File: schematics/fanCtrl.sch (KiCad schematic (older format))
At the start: 0 parts

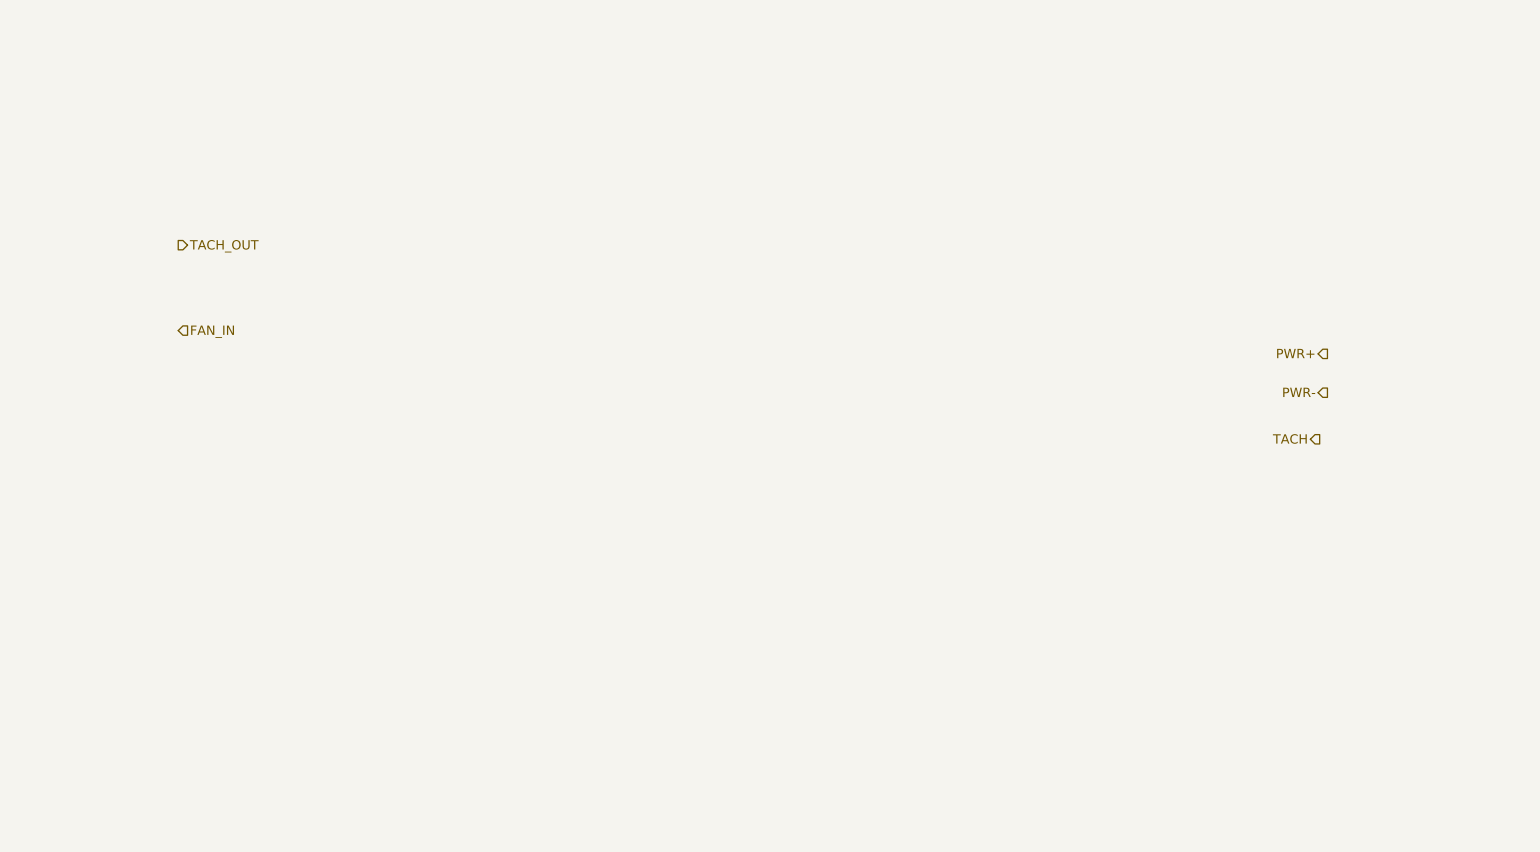
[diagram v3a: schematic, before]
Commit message: added basic current source
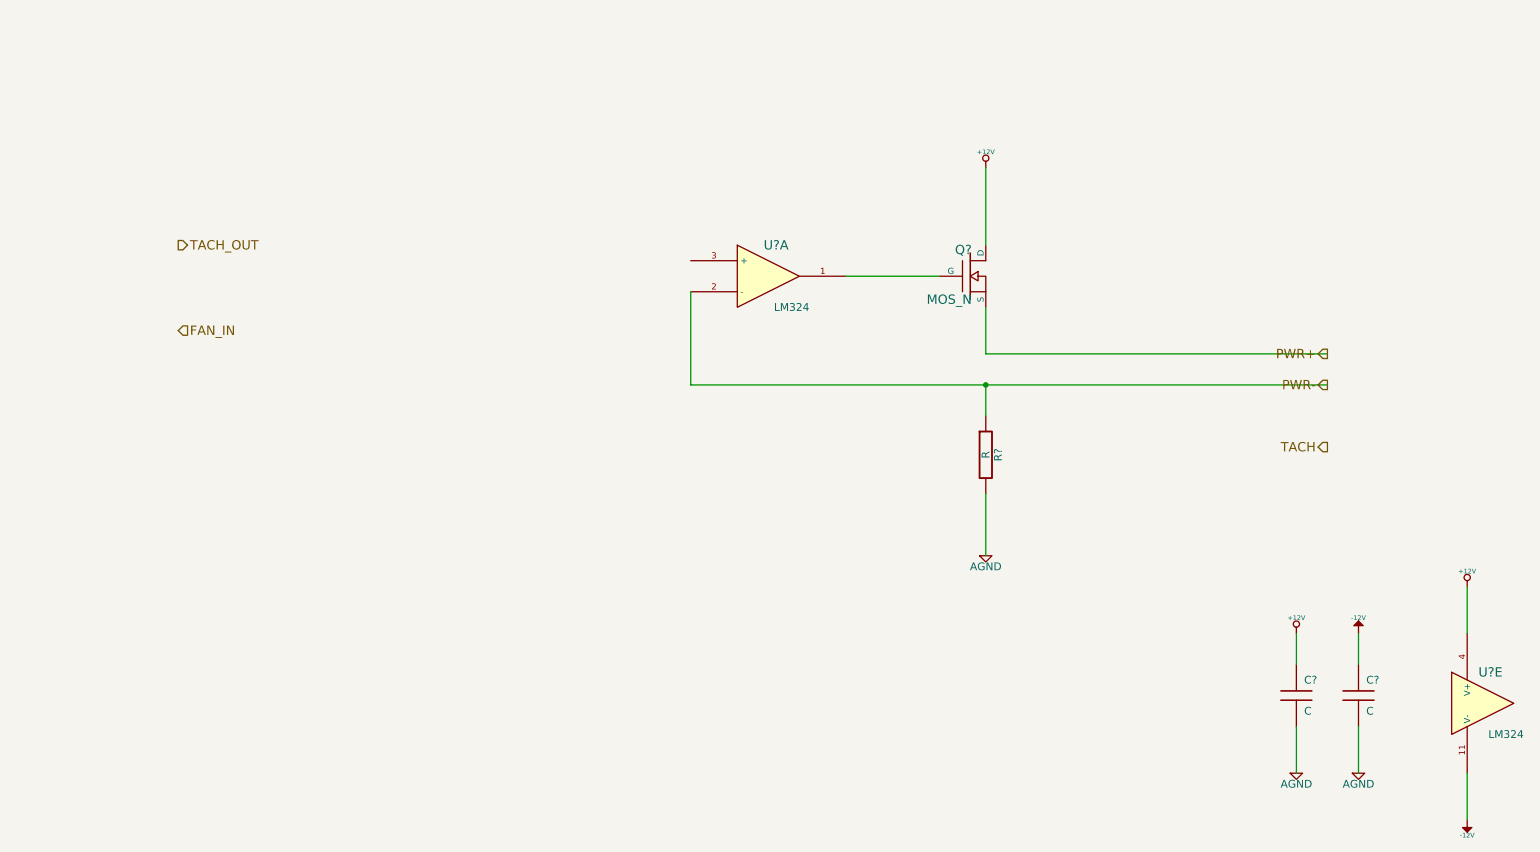
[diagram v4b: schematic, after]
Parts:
- added C? (x2): C, symbol C
- added Q?: MOS_N, symbol MOS_N
- added R?: R, symbol R
- added U? (x2): LM324, symbol LM324
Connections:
- net PWR+: now also Q?.S
- net PWR-: now also R?.1, U?.2 (-)
- new net: Q?.G, U?.1
- new net +12V: C?.1, Q?.D, U?.4 (V+)
- new net -12V: C?.1, U?.11 (V-)
- new net AGND: C?.2, C?.2, R?.2
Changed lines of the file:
@@
-EESchema Schematic File Version 2  date Sat 05 Oct 2013 09:15:56 PM EDT
+EESchema Schematic File Version 2  date Sat 05 Oct 2013 09:39:23 PM EDT
 LIBS:power
 LIBS:device
@@
 Comment4 ""
 $EndDescr
+Wire Wire Line
+	9000 5200 9000 5500
+Wire Wire Line
+	8600 4800 8600 4600
+Wire Wire Line
+	9700 4300 9700 4600
+Connection ~ 6600 3000
+Wire Wire Line
+	4700 2400 4700 3000
+Wire Wire Line
+	4700 3000 8800 3000
+Wire Wire Line
+	6600 3000 6600 3200
+Wire Wire Line
+	6600 1600 6600 2100
+Wire Wire Line
+	6300 2300 5700 2300
+Wire Wire Line
+	8800 2800 6600 2800
+Wire Wire Line
+	6600 2800 6600 2500
+Wire Wire Line
+	6600 4100 6600 3700
+Wire Wire Line
+	9700 5800 9700 5500
+Wire Wire Line
+	9000 4800 9000 4600
+Wire Wire Line
+	8600 5200 8600 5500
+$Comp
+L -12V #PWR?
+U 1 1 5250BF15
+P 9000 4600
+F 0 "#PWR?" H 9000 4730 20  0001 C CNN
+F 1 "-12V" H 9000 4700 30  0000 C CNN
+	1    9000 4600
+	1    0    0    -1
+$EndComp
+$Comp
+L +12V #PWR?
+U 1 1 5250BF10
+P 8600 4600
+F 0 "#PWR?" H 8600 4550 20  0001 C CNN
+F 1 "+12V" H 8600 4700 30  0000 C CNN
+	1    8600 4600
+	1    0    0    -1
+$EndComp
+$Comp
+L AGND #PWR?
+U 1 1 5250BF0B
+P 8600 5500
+F 0 "#PWR?" H 8600 5500 40  0001 C CNN
+F 1 "AGND" H 8600 5430 50  0000 C CNN
+	1    8600 5500
+	1    0    0    -1
+$EndComp
+$Comp
+L AGND #PWR?
+U 1 1 5250BF04
+P 9000 5500
+F 0 "#PWR?" H 9000 5500 40  0001 C CNN
+F 1 "AGND" H 9000 5430 50  0000 C CNN
+	1    9000 5500
+	1    0    0    -1
+$EndComp
+$Comp
+L C C?
+U 1 1 5250BEFF
+P 8600 5000
+F 0 "C?" H 8650 5100 50  0000 L CNN
+F 1 "C" H 8650 4900 50  0000 L CNN
+	1    8600 5000
+	1    0    0    -1
+$EndComp
+$Comp
+L C C?
+U 1 1 5250BEFA
+P 9000 5000
+F 0 "C?" H 9050 5100 50  0000 L CNN
+F 1 "C" H 9050 4900 50  0000 L CNN
+	1    9000 5000
+	1    0    0    -1
+$EndComp
+$Comp
+L -12V #PWR?
+U 1 1 5250BEB5
+P 9700 5800
+F 0 "#PWR?" H 9700 5930 20  0001 C CNN
+F 1 "-12V" H 9700 5900 30  0000 C CNN
+	1    9700 5800
+	1    0    0    1
+$EndComp
+$Comp
+L +12V #PWR?
+U 1 1 5250BE9C
+P 9700 4300
+F 0 "#PWR?" H 9700 4250 20  0001 C CNN
+F 1 "+12V" H 9700 4400 30  0000 C CNN
+	1    9700 4300
+	1    0    0    -1
+$EndComp
+$Comp
+L LM324 U?
+U 5 1 5250BE66
+P 9800 5050
+F 0 "U?" H 9850 5250 60  0000 C CNN
+F 1 "LM324" H 9950 4850 50  0000 C CNN
+	5    9800 5050
+	1    0    0    -1
+$EndComp
+$Comp
+L R R?
+U 1 1 5250BE47
+P 6600 3450
+F 0 "R?" V 6680 3450 50  0000 C CNN
+F 1 "R" V 6600 3450 50  0000 C CNN
+	1    6600 3450
+	1    0    0    -1
+$EndComp
+$Comp
+L AGND #PWR?
+U 1 1 5250BE3B
+P 6600 4100
+F 0 "#PWR?" H 6600 4100 40  0001 C CNN
+F 1 "AGND" H 6600 4030 50  0000 C CNN
+	1    6600 4100
+	1    0    0    -1
+$EndComp
+$Comp
+L +12V #PWR?
+U 1 1 5250BDFB
+P 6600 1600
+F 0 "#PWR?" H 6600 1550 20  0001 C CNN
+F 1 "+12V" H 6600 1700 30  0000 C CNN
+	1    6600 1600
+	1    0    0    -1
+$EndComp
+$Comp
+L MOS_N Q?
+U 1 1 5250BDE8
+P 6500 2300
+F 0 "Q?" H 6510 2470 60  0000 R CNN
+F 1 "MOS_N" H 6510 2150 60  0000 R CNN
+	1    6500 2300
+	1    0    0    -1
+$EndComp
+$Comp
+L LM324 U?
+U 1 1 5250BDB6
+P 5200 2300
+F 0 "U?" H 5250 2500 60  0000 C CNN
+F 1 "LM324" H 5350 2100 50  0000 C CNN
+	1    5200 2300
+	1    0    0    -1
+$EndComp
 Text HLabel 1400 2650 2    60   Input ~ 0
 FAN_IN
 Text HLabel 1400 2100 2    60   Output ~ 0
 TACH_OUT
-Text HLabel 8750 3350 0    60   Output ~ 0
+Text HLabel 8800 3400 0    60   Output ~ 0
 TACH
-Text HLabel 8800 3050 0    60   Output ~ 0
+Text HLabel 8800 3000 0    60   Output ~ 0
 PWR-
 Text HLabel 8800 2800 0    60   Output ~ 0

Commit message: added dac placeholder to fan driver circuit
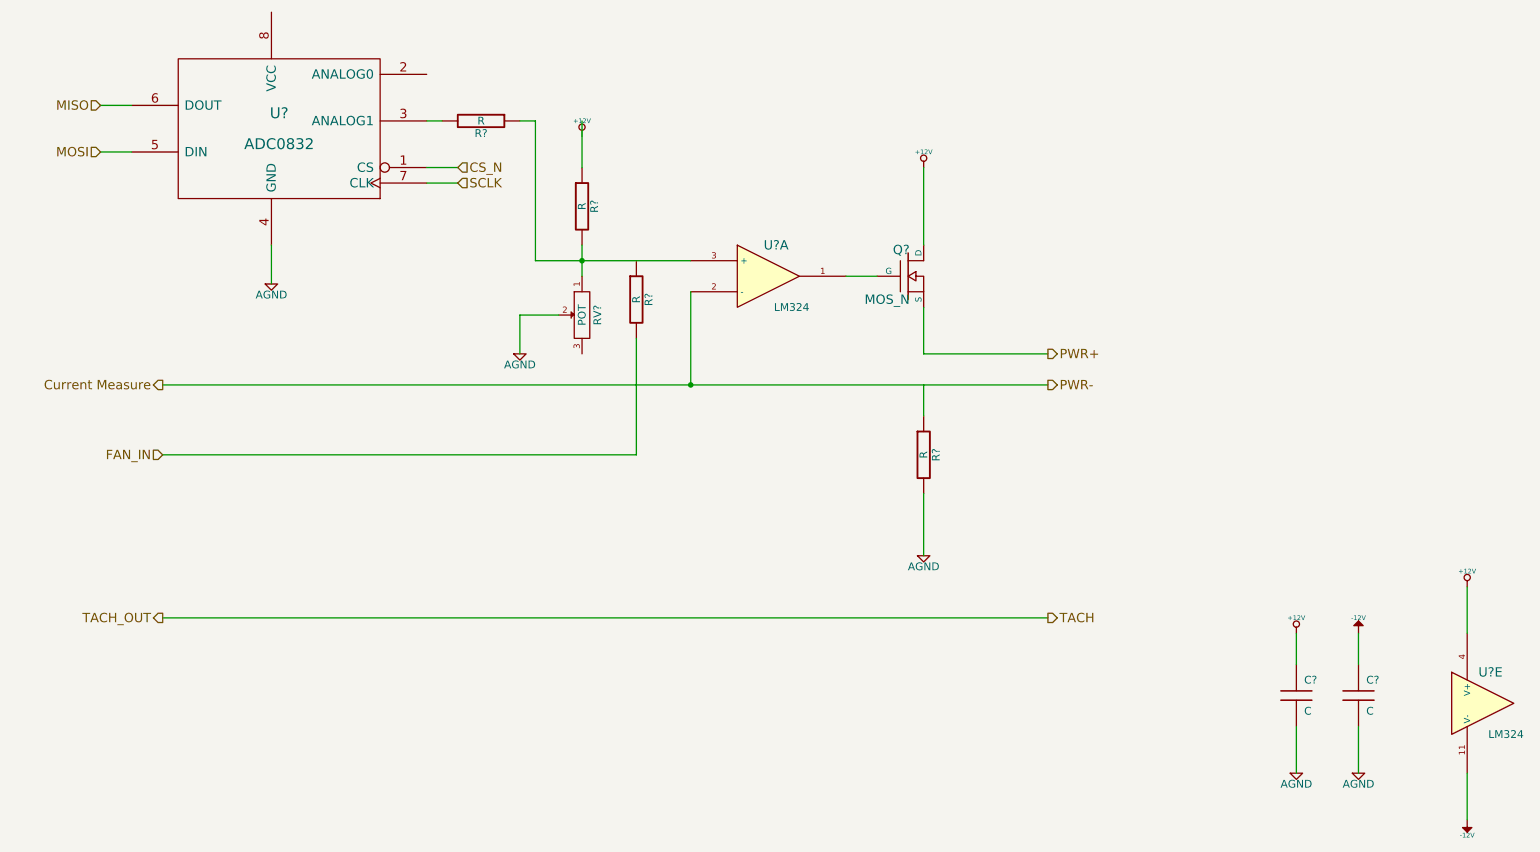
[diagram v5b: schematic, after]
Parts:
- added R? (x3): R, symbol R
- added RV?: POT, symbol POT
- added U?: ADC0832, symbol ADC0832
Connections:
- net labels added: CS_N, Current Measure, MISO, MOSI, SCLK
- wire segments 14 -> 33
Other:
- moved on the sheet: Q?, R?
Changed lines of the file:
@@
-EESchema Schematic File Version 2  date Sat 05 Oct 2013 09:39:23 PM EDT
+EESchema Schematic File Version 2  date Sat 05 Oct 2013 10:01:09 PM EDT
 LIBS:power
 LIBS:device
@@
 $EndDescr
 Wire Wire Line
+	3100 1300 3000 1300
+Wire Wire Line
+	3700 2200 3700 1300
+Wire Wire Line
+	3700 2200 4000 2200
+Wire Wire Line
+	4000 2200 4700 2200
+Wire Wire Line
+	3000 1600 3200 1600
+Wire Wire Line
+	1100 1500 900  1500
+Connection ~ 4700 3000
+Wire Wire Line
+	1300 3000 4700 3000
+Wire Wire Line
+	4700 3000 7000 3000
+Wire Wire Line
+	5900 2300 5700 2300
+Wire Wire Line
+	3850 2550 3600 2550
+Wire Wire Line
+	3600 2550 3600 2800
+Wire Wire Line
 	9000 5200 9000 5500
 Wire Wire Line
@@
 Wire Wire Line
 	9700 4300 9700 4600
-Connection ~ 6600 3000
-Wire Wire Line
-	4700 2400 4700 3000
-Wire Wire Line
-	4700 3000 8800 3000
-Wire Wire Line
-	6600 3000 6600 3200
-Wire Wire Line
-	6600 1600 6600 2100
-Wire Wire Line
-	6300 2300 5700 2300
-Wire Wire Line
-	8800 2800 6600 2800
-Wire Wire Line
-	6600 2800 6600 2500
-Wire Wire Line
-	6600 4100 6600 3700
+Wire Wire Line
+	4700 3000 4700 2400
+Wire Wire Line
+	6200 3000 6200 3200
+Wire Wire Line
+	6200 1600 6200 2100
+Wire Wire Line
+	6200 2500 6200 2800
+Wire Wire Line
+	6200 4100 6200 3700
 Wire Wire Line
 	9700 5800 9700 5500
@@
 Wire Wire Line
 	8600 5200 8600 5500
+Wire Wire Line
+	4000 2300 4000 2200
+Wire Wire Line
+	4000 2200 4000 2100
+Connection ~ 4000 2200
+Wire Wire Line
+	4000 1300 4000 1600
+Wire Wire Line
+	6200 2800 7000 2800
+Wire Wire Line
+	7000 4500 1300 4500
+Wire Wire Line
+	4350 2700 4350 3450
+Wire Wire Line
+	4350 3450 1300 3450
+Wire Wire Line
+	900  1200 1100 1200
+Wire Wire Line
+	3000 1700 3200 1700
+Wire Wire Line
+	2000 2350 2000 2100
+Wire Wire Line
+	3700 1300 3600 1300
+$Comp
+L R R?
+U 1 1 5250C43E
+P 3350 1300
+F 0 "R?" V 3430 1300 50  0000 C CNN
+F 1 "R" V 3350 1300 50  0000 C CNN
+	1    3350 1300
+	0    1    1    0
+$EndComp
+$Comp
+L AGND #PWR?
+U 1 1 5250C41A
+P 2000 2350
+F 0 "#PWR?" H 2000 2350 40  0001 C CNN
+F 1 "AGND" H 2000 2280 50  0000 C CNN
+	1    2000 2350
+	1    0    0    -1
+$EndComp
+$Comp
+L ADC0832 U?
+U 1 1 5250C3A9
+P 2050 1350
+F 0 "U?" H 2050 1450 70  0000 C CNN
+F 1 "ADC0832" H 2050 1251 70  0000 C CNN
+	1    2050 1350
+	-1   0    0    -1
+$EndComp
+Text HLabel 3200 1700 2    60   Input ~ 0
+SCLK
+Text HLabel 3200 1600 2    60   Input ~ 0
+CS_N
+Text HLabel 900  1200 0    60   Input ~ 0
+MISO
+Text HLabel 900  1500 0    60   Input ~ 0
+MOSI
+$Comp
+L R R?
+U 1 1 5250C289
+P 4350 2450
+F 0 "R?" V 4430 2450 50  0000 C CNN
+F 1 "R" V 4350 2450 50  0000 C CNN
+	1    4350 2450
+	1    0    0    -1
+$EndComp
+Text HLabel 1300 3000 0    60   Output ~ 0
+Current Measure
+$Comp
+L +12V #PWR?
+U 1 1 5250BFDD
+P 4000 1400
+F 0 "#PWR?" H 4000 1350 20  0001 C CNN
+F 1 "+12V" H 4000 1500 30  0000 C CNN
+	1    4000 1400
+	1    0    0    -1
+$EndComp
+$Comp
+L AGND #PWR?
+U 1 1 5250BFD0
+P 3600 2800
+F 0 "#PWR?" H 3600 2800 40  0001 C CNN
+F 1 "AGND" H 3600 2730 50  0000 C CNN
+	1    3600 2800
+	1    0    0    -1
+$EndComp
+$Comp
+L POT RV?
+U 1 1 5250BFB3
+P 4000 2550
+F 0 "RV?" H 4000 2450 50  0000 C CNN
+F 1 "POT" H 4000 2550 50  0000 C CNN
+	1    4000 2550
+	0    -1   1    0
+$EndComp
+$Comp
+L R R?
+U 1 1 5250BF84
+P 4000 1850
+F 0 "R?" V 4080 1850 50  0000 C CNN
+F 1 "R" V 4000 1850 50  0000 C CNN
+	1    4000 1850
+	1    0    0    -1
+$EndComp
 $Comp
 L -12V #PWR?
@@
 L R R?
 U 1 1 5250BE47
-P 6600 3450
-F 0 "R?" V 6680 3450 50  0000 C CNN
-F 1 "R" V 6600 3450 50  0000 C CNN
-	1    6600 3450
+P 6200 3450
+F 0 "R?" V 6280 3450 50  0000 C CNN
+F 1 "R" V 6200 3450 50  0000 C CNN
+	1    6200 3450
 	1    0    0    -1
 $EndComp
@@
 L AGND #PWR?
 U 1 1 5250BE3B
-P 6600 4100
-F 0 "#PWR?" H 6600 4100 40  0001 C CNN
-F 1 "AGND" H 6600 4030 50  0000 C CNN
-	1    6600 4100
+P 6200 4100
+F 0 "#PWR?" H 6200 4100 40  0001 C CNN
+F 1 "AGND" H 6200 4030 50  0000 C CNN
+	1    6200 4100
 	1    0    0    -1
 $EndComp
@@
 L +12V #PWR?
 U 1 1 5250BDFB
-P 6600 1600
-F 0 "#PWR?" H 6600 1550 20  0001 C CNN
-F 1 "+12V" H 6600 1700 30  0000 C CNN
-	1    6600 1600
+P 6200 1600
+F 0 "#PWR?" H 6200 1550 20  0001 C CNN
+F 1 "+12V" H 6200 1700 30  0000 C CNN
+	1    6200 1600
 	1    0    0    -1
 $EndComp
@@
 L MOS_N Q?
 U 1 1 5250BDE8
-P 6500 2300
-F 0 "Q?" H 6510 2470 60  0000 R CNN
-F 1 "MOS_N" H 6510 2150 60  0000 R CNN
-	1    6500 2300
+P 6100 2300
+F 0 "Q?" H 6110 2470 60  0000 R CNN
+F 1 "MOS_N" H 6110 2150 60  0000 R CNN
+	1    6100 2300
 	1    0    0    -1
 $EndComp
@@
 	1    0    0    -1
 $EndComp
-Text HLabel 1400 2650 2    60   Input ~ 0
+Text HLabel 1300 3450 0    60   Input ~ 0
 FAN_IN
-Text HLabel 1400 2100 2    60   Output ~ 0
+Text HLabel 1300 4500 0    60   Output ~ 0
 TACH_OUT
-Text HLabel 8800 3400 0    60   Output ~ 0
+Text HLabel 7000 4500 2    60   Output ~ 0
 TACH
-Text HLabel 8800 3000 0    60   Output ~ 0
+Text HLabel 7000 3000 2    60   Output ~ 0
 PWR-
-Text HLabel 8800 2800 0    60   Output ~ 0
+Text HLabel 7000 2800 2    60   Output ~ 0
 PWR+
 $EndSCHEMATC
